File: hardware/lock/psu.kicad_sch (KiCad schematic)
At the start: 9 parts, among them J1 BAT 1S Li-ion, U2 MT3608

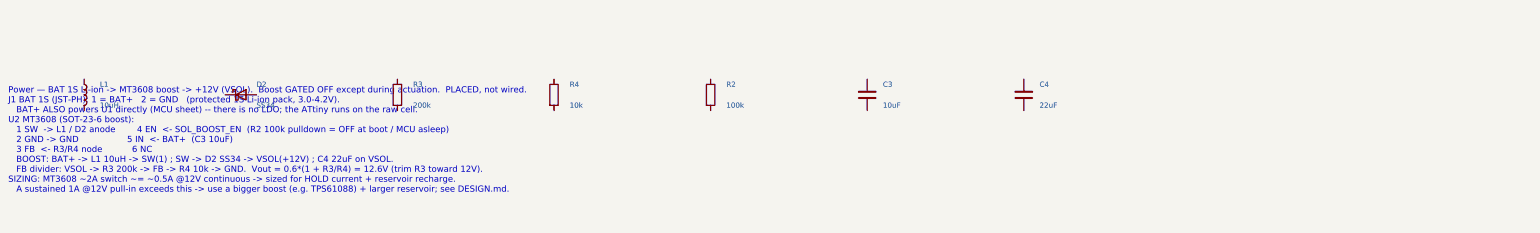
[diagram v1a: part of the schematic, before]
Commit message: lock: servo option, firmware boost/power control, hall sensors, I2C protocol
Checkpoint of the companion lock board evolution:
- I2C link connector -> right-angle 4-pin JST-PH (S4B-PH-K, C157926);
  VCC is No-Connect on the lock (don't bridge the two battery rails).
- Add a parallel servo actuator option (J5) beside the 12V solenoid; one
  fully-populated board can carry both, one active at a time.
- Firmware-selectable boost: BOOST_VSEL (Q2 + R17 switch the FB divider)
  -> 6V (servo, default) or 12V (solenoid).  R4 22k / R17 20k.
- Servo high-side load switch (Q3 P-FET + Q4 driver, SERVO_PWR_EN) with a
  hardware interlock (Q5) that forces servo power OFF whenever boost = 12V,
  so a 12V solenoid pulse can never reach a 6V servo.
- Door/bolt hall sensors (J6/J7, S3B-PH-K) powered from a GPIO (HALL_PWR)
  so they draw ~0uA when the lock sleeps.
- I2C register/command protocol: STATUS (door/bolt/actuator probe, no auth),
  NONCE (read), COMMAND (authenticated UNLOCK/LOCK; LOCK drives a servo to the
  lock angle).  HMAC-SHA1 challenge-response, reuses smalltotp.

All footprints are KiCad-bundled (every part carries a 3D model). Board
regenerates + checks clean (46 components). Docs: hardware/lock/README.md and
DESIGN.md updated.

Co-Authored-By: Claude Opus 4.8 (1M context) <noreply@anthropic.com>
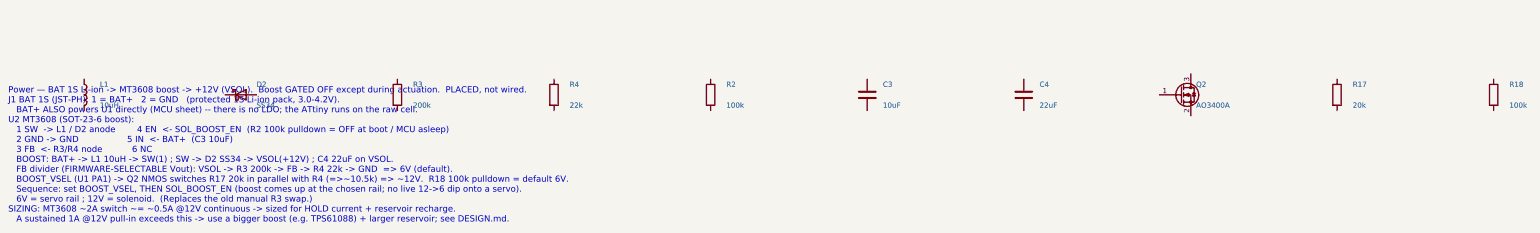
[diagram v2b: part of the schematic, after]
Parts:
- added Q2: AO3400A, Package_TO_SOT_SMD:SOT-23, symbol Transistor_FET:Q_NMOS_GSD
- added R17: 20k, Resistor_SMD:R_0402_1005Metric, symbol Device:R
- added R18: 100k, Resistor_SMD:R_0402_1005Metric, symbol Device:R
- R4: value 10k -> 22k; LCSC C25744 -> C25768
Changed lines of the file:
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@@
 		(instances
 			(project "lock"
-				(path "/e1000000-0000-4000-8000-000000000002/93559584-6df4-4ea3-bcbc-16466d18e9f1"
+				(path "/e1000000-0000-4000-8000-000000000002/2e130db5-a926-472e-84a7-97cbb2425133"
 					(reference "J1")
 					(unit 1)
@@
 		(instances
 			(project "lock"
-				(path "/e1000000-0000-4000-8000-000000000002/93559584-6df4-4ea3-bcbc-16466d18e9f1"
+				(path "/e1000000-0000-4000-8000-000000000002/2e130db5-a926-472e-84a7-97cbb2425133"
 					(reference "U2")
 					(unit 1)
@@
 		(instances
 			(project "lock"
-				(path "/e1000000-0000-4000-8000-000000000002/93559584-6df4-4ea3-bcbc-16466d18e9f1"
+				(path "/e1000000-0000-4000-8000-000000000002/2e130db5-a926-472e-84a7-97cbb2425133"
 					(reference "L1")
 					(unit 1)
@@
 		(instances
 			(project "lock"
-				(path "/e1000000-0000-4000-8000-000000000002/93559584-6df4-4ea3-bcbc-16466d18e9f1"
+				(path "/e1000000-0000-4000-8000-000000000002/2e130db5-a926-472e-84a7-97cbb2425133"
 					(reference "D2")
 					(unit 1)
@@
 		(instances
 			(project "lock"
-				(path "/e1000000-0000-4000-8000-000000000002/93559584-6df4-4ea3-bcbc-16466d18e9f1"
+				(path "/e1000000-0000-4000-8000-000000000002/2e130db5-a926-472e-84a7-97cbb2425133"
 					(reference "R3")
 					(unit 1)
@@
 			(effects (font (size 1.27 1.27)) (justify left))
 		)
-		(property "Value" "10k"
+		(property "Value" "22k"
 			(at 148.5900 124.4600 0)
 			(effects (font (size 1.27 1.27)) (justify left))
@@
 			(effects (font (size 1.27 1.27))) (hide yes)
 		)
-		(property "LCSC" "C25744"
+		(property "LCSC" "C25768"
 			(at 144.7800 121.9200 0)
 			(effects (font (size 1.27 1.27))) (hide yes)
@@
 		(instances
 			(project "lock"
-				(path "/e1000000-0000-4000-8000-000000000002/93559584-6df4-4ea3-bcbc-16466d18e9f1"
+				(path "/e1000000-0000-4000-8000-000000000002/2e130db5-a926-472e-84a7-97cbb2425133"
 					(reference "R4")
 					(unit 1)
@@
 		(instances
 			(project "lock"
-				(path "/e1000000-0000-4000-8000-000000000002/93559584-6df4-4ea3-bcbc-16466d18e9f1"
+				(path "/e1000000-0000-4000-8000-000000000002/2e130db5-a926-472e-84a7-97cbb2425133"
 					(reference "R2")
 					(unit 1)
@@
 		(instances
 			(project "lock"
-				(path "/e1000000-0000-4000-8000-000000000002/93559584-6df4-4ea3-bcbc-16466d18e9f1"
+				(path "/e1000000-0000-4000-8000-000000000002/2e130db5-a926-472e-84a7-97cbb2425133"
 					(reference "C3")
 					(unit 1)
@@
 		(instances
 			(project "lock"
-				(path "/e1000000-0000-4000-8000-000000000002/93559584-6df4-4ea3-bcbc-16466d18e9f1"
+				(path "/e1000000-0000-4000-8000-000000000002/2e130db5-a926-472e-84a7-97cbb2425133"
 					(reference "C4")
 					(unit 1)
@@
 		)
 	)
-	(text "Power — BAT 1S Li-ion -> MT3608 boost -> +12V (VSOL).  Boost GATED OFF except during actuation.  PLACED, not wired.\nJ1 BAT 1S (JST-PH): 1 = BAT+   2 = GND   (protected 1S Li-ion pack, 3.0-4.2V).\n   BAT+ ALSO powers U1 directly (MCU sheet) -- there is no LDO; the ATtiny runs on the raw cell.\nU2 MT3608 (SOT-23-6 boost):\n   1 SW  -> L1 / D2 anode        4 EN  <- SOL_BOOST_EN  (R2 100k pulldown = OFF at boot / MCU asleep)\n   2 GND -> GND                  5 IN  <- BAT+  (C3 10uF)\n   3 FB  <- R3/R4 node           6 NC\n   BOOST: BAT+ -> L1 10uH -> SW(1) ; SW -> D2 SS34 -> VSOL(+12V) ; C4 22uF on VSOL.\n   FB divider: VSOL -> R3 200k -> FB -> R4 10k -> GND.  Vout = 0.6*(1 + R3/R4) = 12.6V (trim R3 toward 12V).\nSIZING: MT3608 ~2A switch ~= ~0.5A @12V continuous -> sized for HOLD current + reservoir recharge.\n   A sustained 1A @12V pull-in exceeds this -> use a bigger boost (e.g. TPS61088) + larger reservoir; see DESIGN.md."
+	(symbol
+		(lib_id "Transistor_FET:Q_NMOS_GSD")
+		(at 297.1800 121.9200 0)
+		(unit 1)
+		(exclude_from_sim no)
+		(in_bom yes)
+		(on_board yes)
+		(dnp no)
+		(property "Reference" "Q2"
+			(at 300.9900 119.3800 0)
+			(effects (font (size 1.27 1.27)) (justify left))
+		)
+		(property "Value" "AO3400A"
+			(at 300.9900 124.4600 0)
+			(effects (font (size 1.27 1.27)) (justify left))
+		)
+		(property "Footprint" "Package_TO_SOT_SMD:SOT-23"
+			(at 297.1800 121.9200 0)
+			(effects (font (size 1.27 1.27))) (hide yes)
+		)
+		(property "Datasheet" "~"
+			(at 297.1800 121.9200 0)
+			(effects (font (size 1.27 1.27))) (hide yes)
+		)
+		(property "LCSC" "C20917"
+			(at 297.1800 121.9200 0)
+			(effects (font (size 1.27 1.27))) (hide yes)
+		)
+		(property "MPN" "AO3400A"
+			(at 297.1800 121.9200 0)
+			(effects (font (size 1.27 1.27))) (hide yes)
+		)
+		(property "Manufacturer" "AOS"
+			(at 297.1800 121.9200 0)
+			(effects (font (size 1.27 1.27))) (hide yes)
+		)
+		(pin "1")
+		(pin "2")
+		(pin "3")
+		(instances
+			(project "lock"
+				(path "/e1000000-0000-4000-8000-000000000002/2e130db5-a926-472e-84a7-97cbb2425133"
+					(reference "Q2")
+					(unit 1)
+				)
+			)
+		)
+	)
+	(symbol
+		(lib_id "Device:R")
+		(at 335.2800 121.9200 0)
+		(unit 1)
+		(exclude_from_sim no)
+		(in_bom yes)
+		(on_board yes)
+		(dnp no)
+		(property "Reference" "R17"
+			(at 339.0900 119.3800 0)
+			(effects (font (size 1.27 1.27)) (justify left))
+		)
+		(property "Value" "20k"
+			(at 339.0900 124.4600 0)
+			(effects (font (size 1.27 1.27)) (justify left))
+		)
+		(property "Footprint" "Resistor_SMD:R_0402_1005Metric"
+			(at 335.2800 121.9200 0)
+			(effects (font (size 1.27 1.27))) (hide yes)
+		)
+		(property "Datasheet" "~"
+			(at 335.2800 121.9200 0)
+			(effects (font (size 1.27 1.27))) (hide yes)
+		)
+		(property "LCSC" "C25765"
+			(at 335.2800 121.9200 0)
+			(effects (font (size 1.27 1.27))) (hide yes)
+		)
+		(pin "1")
+		(pin "2")
+		(instances
+			(project "lock"
+				(path "/e1000000-0000-4000-8000-000000000002/2e130db5-a926-472e-84a7-97cbb2425133"
+					(reference "R17")
+					(unit 1)
+				)
+			)
+		)
+	)
+	(symbol
+		(lib_id "Device:R")
+		(at 373.3800 121.9200 0)
+		(unit 1)
+		(exclude_from_sim no)
+		(in_bom yes)
+		(on_board yes)
+		(dnp no)
+		(property "Reference" "R18"
+			(at 377.1900 119.3800 0)
+			(effects (font (size 1.27 1.27)) (justify left))
+		)
+		(property "Value" "100k"
+			(at 377.1900 124.4600 0)
+			(effects (font (size 1.27 1.27)) (justify left))
+		)
+		(property "Footprint" "Resistor_SMD:R_0402_1005Metric"
+			(at 373.3800 121.9200 0)
+			(effects (font (size 1.27 1.27))) (hide yes)
+		)
+		(property "Datasheet" "~"
+			(at 373.3800 121.9200 0)
+			(effects (font (size 1.27 1.27))) (hide yes)
+		)
+		(property "LCSC" "C25741"
+			(at 373.3800 121.9200 0)
+			(effects (font (size 1.27 1.27))) (hide yes)
+		)
+		(pin "1")
+		(pin "2")
+		(instances
+			(project "lock"
+				(path "/e1000000-0000-4000-8000-000000000002/2e130db5-a926-472e-84a7-97cbb2425133"
+					(reference "R18")
+					(unit 1)
+				)
+			)
+		)
+	)
+	(text "Power — BAT 1S Li-ion -> MT3608 boost -> +12V (VSOL).  Boost GATED OFF except during actuation.  PLACED, not wired.\nJ1 BAT 1S (JST-PH): 1 = BAT+   2 = GND   (protected 1S Li-ion pack, 3.0-4.2V).\n   BAT+ ALSO powers U1 directly (MCU sheet) -- there is no LDO; the ATtiny runs on the raw cell.\nU2 MT3608 (SOT-23-6 boost):\n   1 SW  -> L1 / D2 anode        4 EN  <- SOL_BOOST_EN  (R2 100k pulldown = OFF at boot / MCU asleep)\n   2 GND -> GND                  5 IN  <- BAT+  (C3 10uF)\n   3 FB  <- R3/R4 node           6 NC\n   BOOST: BAT+ -> L1 10uH -> SW(1) ; SW -> D2 SS34 -> VSOL(+12V) ; C4 22uF on VSOL.\n   FB divider (FIRMWARE-SELECTABLE Vout): VSOL -> R3 200k -> FB -> R4 22k -> GND  => 6V (default).\n   BOOST_VSEL (U1 PA1) -> Q2 NMOS switches R17 20k in parallel with R4 (=>~10.5k) => ~12V.  R18 100k pulldown = default 6V.\n   Sequence: set BOOST_VSEL, THEN SOL_BOOST_EN (boost comes up at the chosen rail; no live 12->6 dip onto a servo).\n   6V = servo rail ; 12V = solenoid.  (Replaces the old manual R3 swap.)\nSIZING: MT3608 ~2A switch ~= ~0.5A @12V continuous -> sized for HOLD current + reservoir recharge.\n   A sustained 1A @12V pull-in exceeds this -> use a bigger boost (e.g. TPS61088) + larger reservoir; see DESIGN.md."
 		(exclude_from_sim no)
 		(at 12.00 120.00 0)

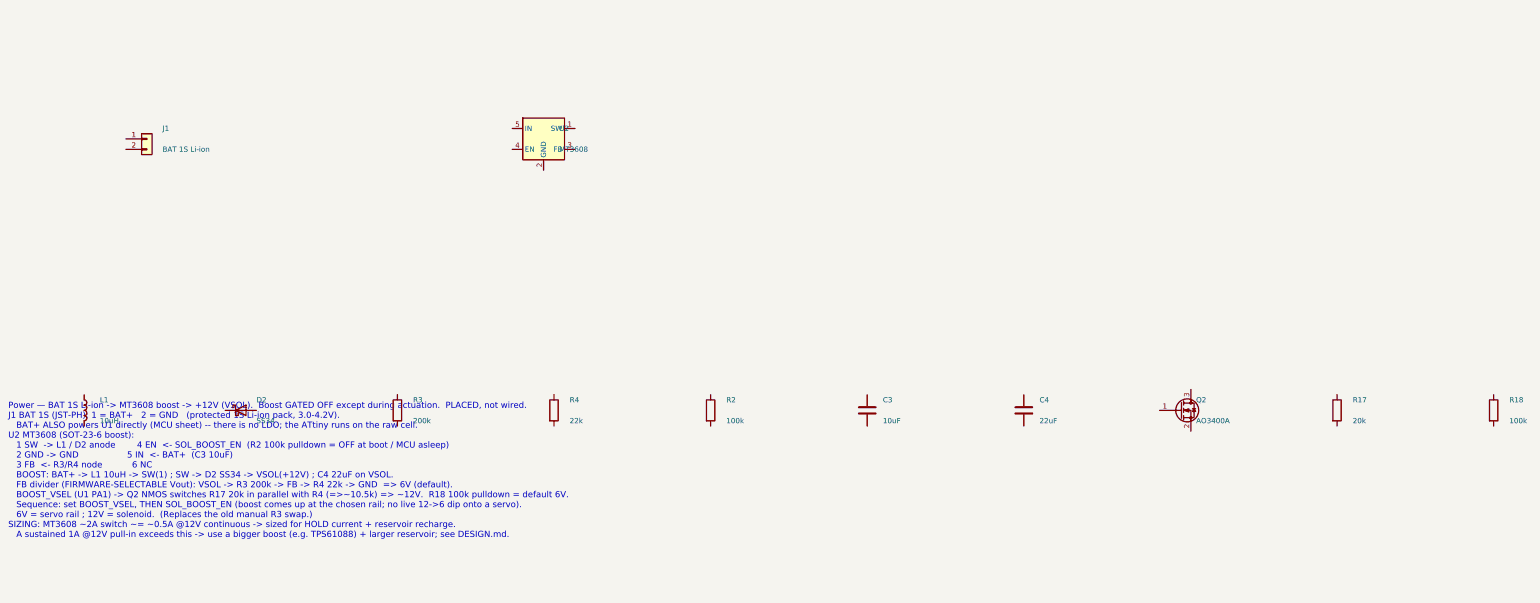
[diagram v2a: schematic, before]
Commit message: lock: second servo output, clearer wiring notes, start PCB layout
- Add a second servo output (J8 + SERVO_SIG2 on PB4, R24/R25) sharing the
  VSERVO rail and the load-switch/interlock -- e.g. a dual-latch lock.
- Rewrite the per-sheet wiring notes (MCU/PWR/DRV) from prose into terse
  pin -> net maps: one line per part, every pin = its net, with a NETS IN
  header for cross-sheet signals. Rationale stays in the README.
- kschgen: park the wiring note below all placed components so the text no
  longer overlaps symbols (computed from the last component row).
- Start the lock PCB layout (hardware/lock/lock.kicad_pcb).

Board regenerates + checks clean (49 components; all footprints carry 3D models).

Co-Authored-By: Claude Opus 4.8 (1M context) <noreply@anthropic.com>
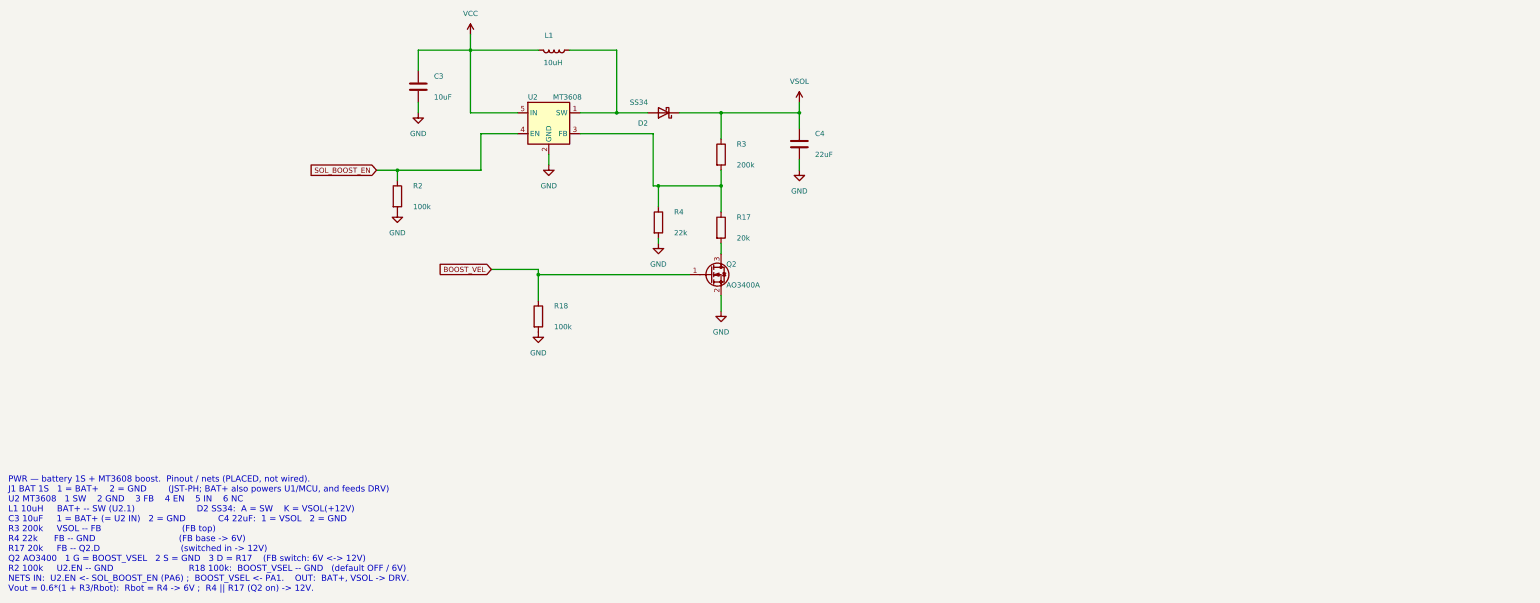
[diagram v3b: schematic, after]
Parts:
- removed J1: BAT 1S Li-ion, Connector_JST:JST_PH_S2B-PH-K_1x02_P2.00mm_Horizontal, symbol Connector_Generic:Conn_01x02
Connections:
- net BOOST_VEL: now reaches R18.1
- net BOOST_VEL: now also Q2.1 (G)
- net GND: now reaches R18.2
- net GND: now also C3.2, C4.2, Q2.2 (S), R2.2, R4.2, U2.2 (GND)
- net at R17.1: now also R3.2, R4.1, U2.3 (FB)
- net at R17.2: now also Q2.3 (D)
- net VCC: now reaches C3.1
- net VCC: now also L1.2, U2.5 (IN)
- net at L1.1: now also D2.2 (A), U2.1 (SW)
- net SOL_BOOST_EN: now reaches R2.1
- net SOL_BOOST_EN: now also U2.4 (EN)
- net VSOL: now reaches C4.1
- net VSOL: now also D2.1 (K), R3.1
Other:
- note added: "PWR — battery 1S + MT3608 boost. Pinout / nets (PLACED, not wired). J1 BAT 1S 1 = BAT+ 2 = GND (JST-PH; BAT+ also powers U1/MCU, and feeds DRV) U2 MT3608 1 SW 2 GND 3 FB 4 EN 5 IN 6 NC L1 10uH BAT+ -- SW (U2.1) D2 SS34: A = SW K = VSOL(+12V) C3 10uF 1 = BAT+ (= U2 IN) 2 = GND C4 22uF: 1 = VSOL 2 = GND R3 200k VSOL -- FB (FB top) R4 22k FB -- GND (FB base -> 6V) R17 20k FB -- Q2.D (switched in -> 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"
- note removed: "Power — BAT 1S Li-ion -> MT3608 boost -> +12V (VSOL). Boost GATED OFF except during actuation. PLACED, not wired. J1 BAT 1S (JST-PH): 1 = BAT+ 2 = GND (protected 1S Li-ion pack, 3.0-4.2V). BAT+ ALSO powers U1 directly (MCU sheet) -- there is no LDO; the ATtiny runs on the raw cell. U2 MT3608 (SOT-23-6 boost): 1 SW -> L1 / D2 anode 4 EN <- SOL_BOOST_EN (R2 100k pulldown = OFF at boot / MCU asleep)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"

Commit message: lock: power from I2C connector (VSYS), LED on PC3; route board; ephemerkey J2=VSYS
Power move: the lock has NO local battery (J1 removed) — VCC and the boost/
actuator draw come from ephemerkey's VSYS rail over the I2C connector (J2.2).
- ephemerkey: J2.2 = VSYS (was +3V3); manifest note + DESIGN.md updated, regenerated.
- lock: README interface/architecture/BOM + servo source (R13=VSOL / R14=VSYS,
  no more VBAT) updated to match the as-wired board.
- Caveat documented: a 12V solenoid pull-in (~3-4A) exceeds a JST-PH contact and
  ephemerkey's load-share; favor the 6V servo / low-duty, or a dedicated feed.
- I2C pull-ups stay on ephemerkey at +3V3 (STM32 pins not >3.6V tolerant).

LED move: status LED (D1) is driven by PC3, not PA3 (PA3 now spare). Docs + manifest.

lock schematic + PCB are now hand-wired and fully routed (DRC: 0 unconnected,
0 schematic-parity). Manifest marked REFERENCE-OF-RECORD — do not regenerate
(would destroy the wiring). Verified with KiCad's own kicad-cli ERC/DRC.

Pending (owner fixing): PWR_FLAGs on VCC/GND, NC flags on unused pins, J6/J7 GND
thermal relief, minor stub/silk cleanups.

Co-Authored-By: Claude Opus 4.8 (1M context) <noreply@anthropic.com>
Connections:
- net BOOST_VEL renamed BOOST_VSEL
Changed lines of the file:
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@@
 		)
 	)
-	(global_label "BOOST_VEL"
+	(global_label "BOOST_VSEL"
 		(shape input)
 		(at 129.54 87.63 180)
@@
 		)
 		(property "Intersheetrefs" "${INTERSHEET_REFS}"
-			(at 116.2134 87.63 0)
+			(at 115.0039 87.63 0)
 			(show_name no)
 			(do_not_autoplace no)
